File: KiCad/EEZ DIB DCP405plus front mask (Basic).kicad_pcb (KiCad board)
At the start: 2 copper layers, 35 x 111.5 mm, 7 parts

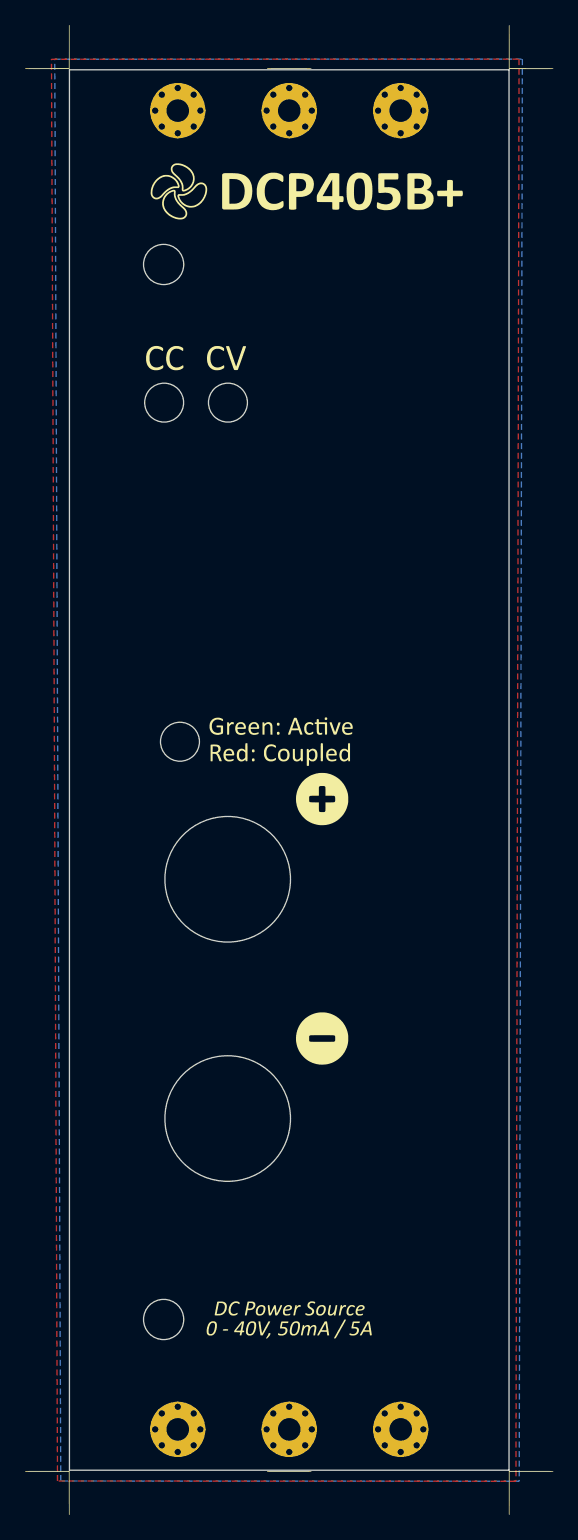
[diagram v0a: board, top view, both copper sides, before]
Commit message: Resized front masks
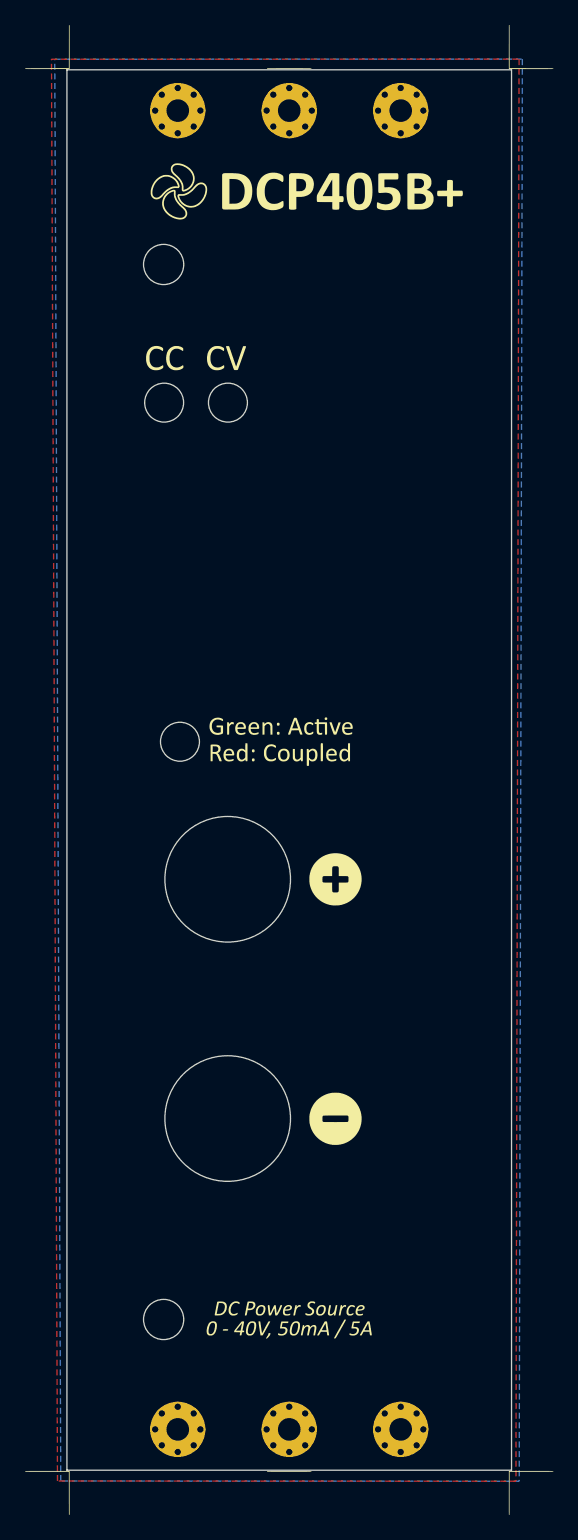
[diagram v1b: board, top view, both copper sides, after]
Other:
- board size 35 x 111.5 mm -> 35.4 x 111.5 mm
